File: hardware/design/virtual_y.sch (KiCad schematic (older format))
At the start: 4 parts, among them P6 PAD_SMD

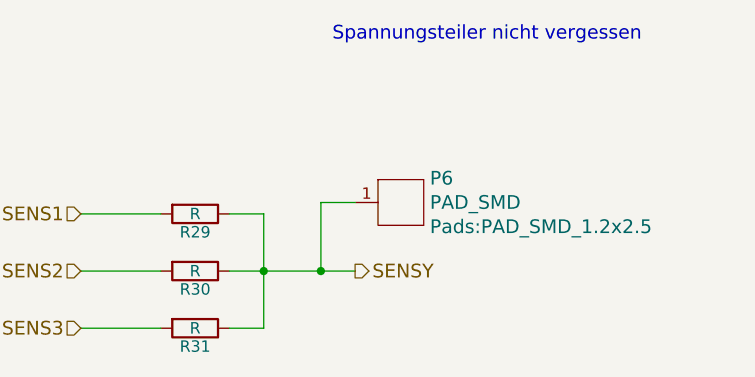
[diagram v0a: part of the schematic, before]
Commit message: Six-phase power stage.
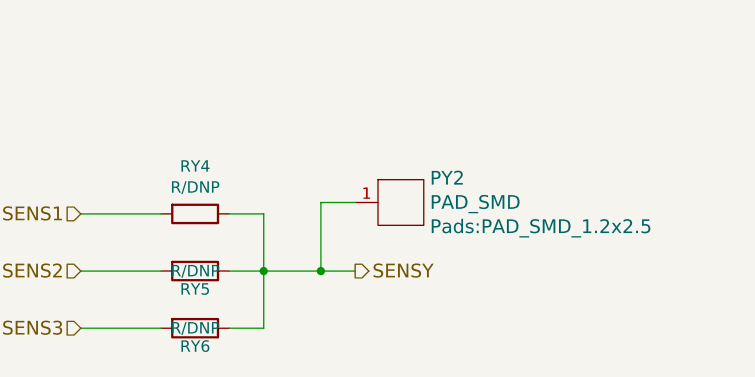
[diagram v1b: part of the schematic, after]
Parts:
- RY1: renamed from R29; value R -> R/DNP
- RY2: renamed from R30; value R -> R/DNP
- RY3: renamed from R31; value R -> R/DNP
- renumbered P6 to PY1
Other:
- note removed: "Spannungsteiler nicht vergessen"
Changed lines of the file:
@@
 $Descr A4 11693 8268
 encoding utf-8
-Sheet 6 6
+Sheet 6 12
 Title ""
 Date ""
@@
 SENSY
 $Comp
-L R R29
+L R RY1
 U 1 1 55E2B8A9
 P 4500 3100
-F 0 "R29" V 4580 3100 50  0000 C CNN
-F 1 "R" V 4500 3100 50  0000 C CNN
+AR Path="/55DFCB16/55E2B8A9" Ref="RY1"  Part="1"
+AR Path="/56BBABF4/55E2B8A9" Ref="RY4"  Part="1"
+F 0 "RY4" V 4292 3100 50  0000 C CNN
+F 1 "R/DNP" V 4384 3100 50  0000 C CNN
 F 2 "Resistors_SMD:R_0603_HandSoldering" V 4430 3100 30  0001 C CNN
 F 3 "" H 4500 3100 30  0000 C CNN
@@
 $EndComp
 $Comp
-L R R30
+L R RY2
 U 1 1 55E2B8E8
 P 4500 3350
-F 0 "R30" V 4580 3350 50  0000 C CNN
-F 1 "R" V 4500 3350 50  0000 C CNN
+AR Path="/55DFCB16/55E2B8E8" Ref="RY2"  Part="1"
+AR Path="/56BBABF4/55E2B8E8" Ref="RY5"  Part="1"
+F 0 "RY5" V 4580 3350 50  0000 C CNN
+F 1 "R/DNP" V 4500 3350 50  0000 C CNN
 F 2 "Resistors_SMD:R_0603_HandSoldering" V 4430 3350 30  0001 C CNN
 F 3 "" H 4500 3350 30  0000 C CNN
@@
 $EndComp
 $Comp
-L R R31
+L R RY3
 U 1 1 55E2B905
 P 4500 3600
-F 0 "R31" V 4580 3600 50  0000 C CNN
-F 1 "R" V 4500 3600 50  0000 C CNN
+AR Path="/55DFCB16/55E2B905" Ref="RY3"  Part="1"
+AR Path="/56BBABF4/55E2B905" Ref="RY6"  Part="1"
+F 0 "RY6" V 4580 3600 50  0000 C CNN
+F 1 "R/DNP" V 4500 3600 50  0000 C CNN
 F 2 "Resistors_SMD:R_0603_HandSoldering" V 4430 3600 30  0001 C CNN
 F 3 "" H 4500 3600 30  0000 C CNN
@@
 	4800 3600 4650 3600
 $Comp
-L PAD_SMD P6
+L PAD_SMD PY1
 U 1 1 56A8F597
 P 5400 3050
-F 0 "P6" H 5527 3156 60  0000 L CNN
+AR Path="/55DFCB16/56A8F597" Ref="PY1"  Part="1"
+AR Path="/56BBABF4/56A8F597" Ref="PY2"  Part="1"
+F 0 "PY2" H 5527 3156 60  0000 L CNN
 F 1 "PAD_SMD" H 5527 3050 60  0000 L CNN
 F 2 "Pads:PAD_SMD_1.2x2.5" H 5527 2944 60  0000 L CNN
@@
 	5050 3050 5050 3350
 Connection ~ 5050 3350
-Text Notes 5100 2350 0    60   ~ 0
-Spannungsteiler nicht vergessen
 $EndSCHEMATC

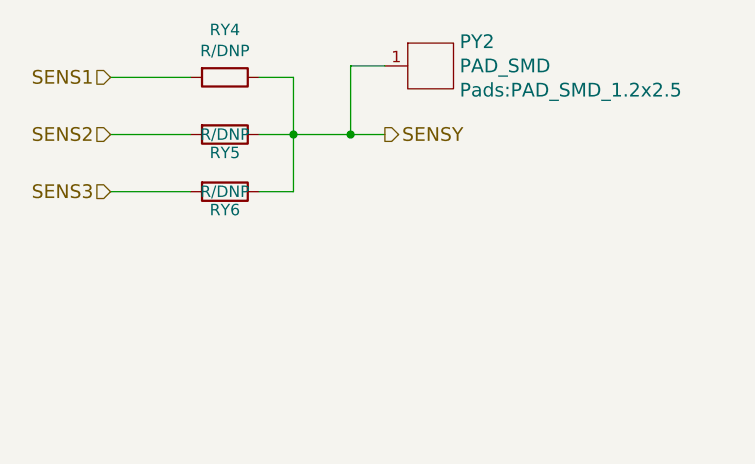
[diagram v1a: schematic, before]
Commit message: TODO: Routing of the DSBL-signals.
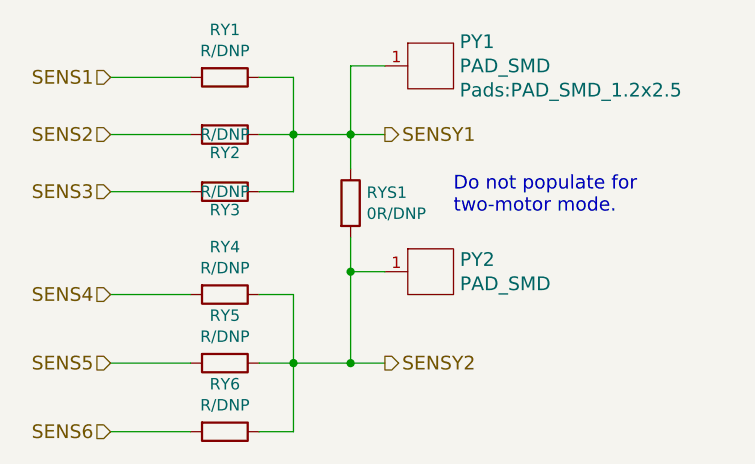
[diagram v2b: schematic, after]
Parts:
- added PY2: PAD_SMD, Pads:PAD_SMD_1.2x2.5, symbol PAD_SMD
- added RY4, RY5, RY6: R/DNP, Resistors_SMD:R_0603_HandSoldering, symbol R
- added RYS1: 0R/DNP, Resistors_SMD:R_0603_HandSoldering, symbol R
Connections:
- net SENSY renamed SENSY1
- net SENSY1: now also RYS1.1
- new net SENS4: RY4.2
- new net SENS5: RY5.2
- new net SENS6: RY6.2
- new net SENSY2: PY2.1 (PAD), RY4.1, RY5.1, RY6.1, RYS1.2
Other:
- note added: "Do not populate for\ntwo-motor mode."
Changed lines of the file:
@@
 $Descr A4 11693 8268
 encoding utf-8
-Sheet 6 12
+Sheet 6 11
 Title ""
 Date ""
@@
 SENS3
 Text HLabel 5200 3350 2    60   Output ~ 0
-SENSY
+SENSY1
 $Comp
 L R RY1
@@
 AR Path="/55DFCB16/55E2B8A9" Ref="RY1"  Part="1"
 AR Path="/56BBABF4/55E2B8A9" Ref="RY4"  Part="1"
-F 0 "RY4" V 4292 3100 50  0000 C CNN
+F 0 "RY1" V 4292 3100 50  0000 C CNN
 F 1 "R/DNP" V 4384 3100 50  0000 C CNN
 F 2 "Resistors_SMD:R_0603_HandSoldering" V 4430 3100 30  0001 C CNN
@@
 AR Path="/55DFCB16/55E2B8E8" Ref="RY2"  Part="1"
 AR Path="/56BBABF4/55E2B8E8" Ref="RY5"  Part="1"
-F 0 "RY5" V 4580 3350 50  0000 C CNN
+F 0 "RY2" V 4580 3350 50  0000 C CNN
 F 1 "R/DNP" V 4500 3350 50  0000 C CNN
 F 2 "Resistors_SMD:R_0603_HandSoldering" V 4430 3350 30  0001 C CNN
@@
 AR Path="/55DFCB16/55E2B905" Ref="RY3"  Part="1"
 AR Path="/56BBABF4/55E2B905" Ref="RY6"  Part="1"
-F 0 "RY6" V 4580 3600 50  0000 C CNN
+F 0 "RY3" V 4580 3600 50  0000 C CNN
 F 1 "R/DNP" V 4500 3600 50  0000 C CNN
 F 2 "Resistors_SMD:R_0603_HandSoldering" V 4430 3600 30  0001 C CNN
@@
 AR Path="/55DFCB16/56A8F597" Ref="PY1"  Part="1"
 AR Path="/56BBABF4/56A8F597" Ref="PY2"  Part="1"
-F 0 "PY2" H 5527 3156 60  0000 L CNN
+F 0 "PY1" H 5527 3156 60  0000 L CNN
 F 1 "PAD_SMD" H 5527 3050 60  0000 L CNN
 F 2 "Pads:PAD_SMD_1.2x2.5" H 5527 2944 60  0000 L CNN
@@
 	5200 3050 5050 3050
 Wire Wire Line
-	5050 3050 5050 3350
+	5050 3050 5050 3500
 Connection ~ 5050 3350
+$Comp
+L PAD_SMD PY2
+U 1 1 56CBA2A8
+P 5400 3950
+F 0 "PY2" H 5528 4003 60  0000 L CNN
+F 1 "PAD_SMD" H 5528 3897 60  0000 L CNN
+F 2 "Pads:PAD_SMD_1.2x2.5" H 5400 3700 60  0001 C CNN
+F 3 "" H 5400 3800 60  0000 C CNN
+	1    5400 3950
+	1    0    0    -1
+$EndComp
+$Comp
+L R RY4
+U 1 1 56CBA2E3
+P 4500 4050
+F 0 "RY4" V 4292 4050 50  0000 C CNN
+F 1 "R/DNP" V 4384 4050 50  0000 C CNN
+F 2 "Resistors_SMD:R_0603_HandSoldering" V 4430 4050 50  0001 C CNN
+F 3 "" H 4500 4050 50  0000 C CNN
+	1    4500 4050
+	0    1    1    0
+$EndComp
+$Comp
+L R RY5
+U 1 1 56CBA350
+P 4500 4350
+F 0 "RY5" V 4292 4350 50  0000 C CNN
+F 1 "R/DNP" V 4384 4350 50  0000 C CNN
+F 2 "Resistors_SMD:R_0603_HandSoldering" V 4430 4350 50  0001 C CNN
+F 3 "" H 4500 4350 50  0000 C CNN
+	1    4500 4350
+	0    1    1    0
+$EndComp
+$Comp
+L R RY6
+U 1 1 56CBA38A
+P 4500 4650
+F 0 "RY6" V 4292 4650 50  0000 C CNN
+F 1 "R/DNP" V 4384 4650 50  0000 C CNN
+F 2 "Resistors_SMD:R_0603_HandSoldering" V 4430 4650 50  0001 C CNN
+F 3 "" H 4500 4650 50  0000 C CNN
+	1    4500 4650
+	0    1    1    0
+$EndComp
+Text HLabel 4000 4050 0    60   Input ~ 0
+SENS4
+Text HLabel 4000 4350 0    60   Input ~ 0
+SENS5
+Text HLabel 4000 4650 0    60   Input ~ 0
+SENS6
+$Comp
+L R RYS1
+U 1 1 56CBA751
+P 5050 3650
+F 0 "RYS1" H 5120 3696 50  0000 L CNN
+F 1 "0R/DNP" H 5120 3604 50  0000 L CNN
+F 2 "Resistors_SMD:R_0603_HandSoldering" V 4980 3650 50  0001 C CNN
+F 3 "" H 5050 3650 50  0000 C CNN
+	1    5050 3650
+	1    0    0    -1
+$EndComp
+Wire Wire Line
+	4000 4050 4350 4050
+Wire Wire Line
+	4000 4350 4350 4350
+Wire Wire Line
+	4000 4650 4350 4650
+Wire Wire Line
+	4650 4050 4800 4050
+Wire Wire Line
+	4800 4050 4800 4650
+Wire Wire Line
+	4650 4350 5200 4350
+Wire Wire Line
+	4800 4650 4650 4650
+Connection ~ 4800 4350
+Wire Wire Line
+	5200 3950 5050 3950
+Wire Wire Line
+	5050 3800 5050 4350
+Text HLabel 5200 4350 2    60   Output ~ 0
+SENSY2
+Connection ~ 5050 4350
+Connection ~ 5050 3950
+Text Notes 5500 3700 0    60   ~ 0
+Do not populate for\ntwo-motor mode.
 $EndSCHEMATC

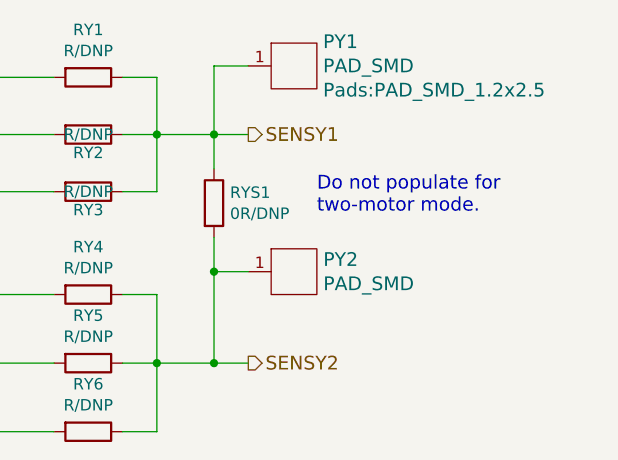
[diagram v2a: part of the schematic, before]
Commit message: Next step: connect GND and PWRGND.
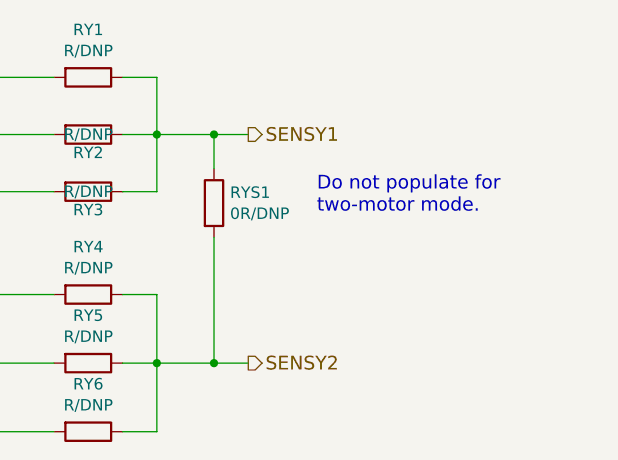
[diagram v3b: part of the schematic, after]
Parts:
- removed PY1, PY2: PAD_SMD, Pads:PAD_SMD_1.2x2.5, symbol PAD_SMD
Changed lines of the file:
@@
 $Descr A4 11693 8268
 encoding utf-8
-Sheet 6 11
+Sheet 5 11
 Title ""
 Date ""
@@
 Wire Wire Line
 	4800 3600 4650 3600
-$Comp
-L PAD_SMD PY1
-U 1 1 56A8F597
-P 5400 3050
-AR Path="/55DFCB16/56A8F597" Ref="PY1"  Part="1"
-AR Path="/56BBABF4/56A8F597" Ref="PY2"  Part="1"
-F 0 "PY1" H 5527 3156 60  0000 L CNN
-F 1 "PAD_SMD" H 5527 3050 60  0000 L CNN
-F 2 "Pads:PAD_SMD_1.2x2.5" H 5527 2944 60  0000 L CNN
-F 3 "" H 5400 2900 60  0000 C CNN
-	1    5400 3050
-	1    0    0    -1
-$EndComp
-Wire Wire Line
-	5200 3050 5050 3050
-Wire Wire Line
-	5050 3050 5050 3500
 Connection ~ 5050 3350
-$Comp
-L PAD_SMD PY2
-U 1 1 56CBA2A8
-P 5400 3950
-F 0 "PY2" H 5528 4003 60  0000 L CNN
-F 1 "PAD_SMD" H 5528 3897 60  0000 L CNN
-F 2 "Pads:PAD_SMD_1.2x2.5" H 5400 3700 60  0001 C CNN
-F 3 "" H 5400 3800 60  0000 C CNN
-	1    5400 3950
-	1    0    0    -1
-$EndComp
 $Comp
 L R RY4
@@
 	4800 4650 4650 4650
 Connection ~ 4800 4350
-Wire Wire Line
-	5200 3950 5050 3950
-Wire Wire Line
-	5050 3800 5050 4350
 Text HLabel 5200 4350 2    60   Output ~ 0
 SENSY2
 Connection ~ 5050 4350
-Connection ~ 5050 3950
 Text Notes 5500 3700 0    60   ~ 0
 Do not populate for\ntwo-motor mode.
+Wire Wire Line
+	5050 3500 5050 3350
+Wire Wire Line
+	5050 3800 5050 4350
 $EndSCHEMATC

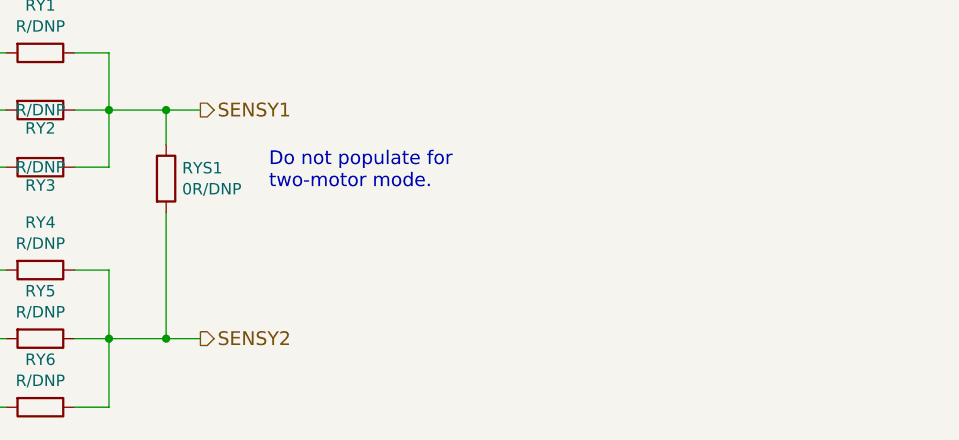
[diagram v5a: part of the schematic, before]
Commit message: Included option for filtering sensev through small caps on RYSx
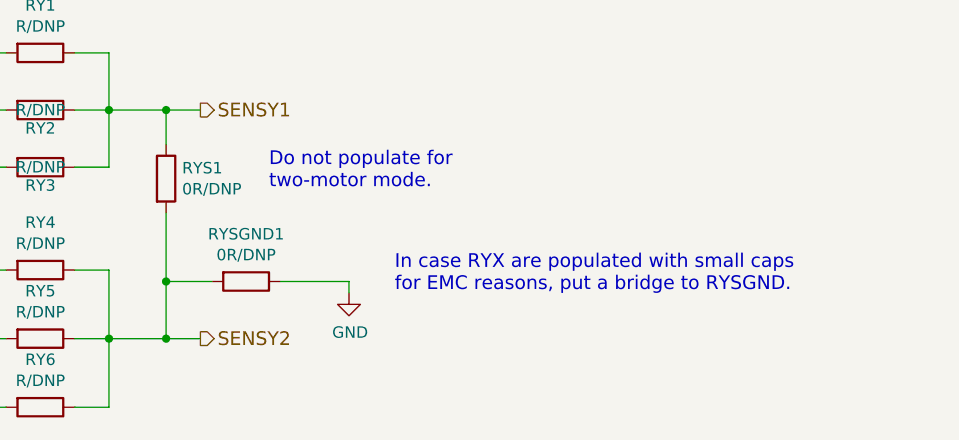
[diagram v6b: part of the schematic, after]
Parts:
- added RYSGND1: 0R/DNP, Resistors_SMD:R_0402, symbol R
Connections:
- net SENSY2: now also RYSGND1.2
- new net GND: RYSGND1.1
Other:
- note added: "In case RYX are populated with small caps\nfor EMC reasons, put a bridge to RYSGND."
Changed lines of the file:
@@
 Wire Wire Line
 	5050 3800 5050 4350
+$Comp
+L R RYSGND1
+U 1 1 57935AF7
+P 5400 4100
+F 0 "RYSGND1" V 5193 4100 50  0000 C CNN
+F 1 "0R/DNP" V 5284 4100 50  0000 C CNN
+F 2 "Resistors_SMD:R_0402" V 5330 4100 50  0001 C CNN
+F 3 "" H 5400 4100 50  0000 C CNN
+	1    5400 4100
+	0    1    1    0
+$EndComp
+Wire Wire Line
+	5250 4100 5050 4100
+Connection ~ 5050 4100
+$Comp
+L GND #PWR037
+U 1 1 57935C8D
+P 5850 4150
+F 0 "#PWR037" H 5850 3900 50  0001 C CNN
+F 1 "GND" H 5855 3977 50  0000 C CNN
+F 2 "" H 5850 4150 50  0000 C CNN
+F 3 "" H 5850 4150 50  0000 C CNN
+	1    5850 4150
+	1    0    0    -1
+$EndComp
+Wire Wire Line
+	5550 4100 5850 4100
+Wire Wire Line
+	5850 4100 5850 4150
+Text Notes 6050 4150 0    60   ~ 0
+In case RYX are populated with small caps\nfor EMC reasons, put a bridge to RYSGND.
 $EndSCHEMATC
